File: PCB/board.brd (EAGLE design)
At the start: 30 x 30 mm, 13 parts, among them IC1 W25Q32JVSSIQ, J1 USB-TYPE-C-31-M-17, U1 ESP8266EX, U2 AMS1117_SOT223, Y2 CRYSTAL-26MHZ

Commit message: schematics
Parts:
- removed Y2: CRYSTAL-26MHZ, angrypig7-Clocks:CRYSTAL-SMD-3.2X2.5MM
- added C10: 100nF, angrypig7-RCL:C0402
- added C11, C12: 1uF, angrypig7-RCL:C0402
- added C13: 10uF, angrypig7-RCL:C0402
- added C14: 5.6pF, angrypig7-RCL:C0402
- added C8: 20pF, angrypig7-RCL:C0402
- added R1: (no value), angrypig7-RCL:R0402
- added R2: 12k, angrypig7-RCL:R0402
- added U3: ESP01_PINOUT, angrypig7-IC:ESP01-PINOUT
- added X1: SMA, angrypig7-Connectors:SMA-END-LAUNCH-2
- added Y1: 26Mhz, angrypig7-Clocks:CRYSTAL-SMD-3.2X2.5MM
- C9: value 1uF -> 20pF
- moved IC1 11.3 mm to (15.2, 11.6), turned to 0 degrees
- moved C9 7.11 mm to (20.3, 22.0), turned to 180 degrees
- moved C6 6.13 mm to (3.81, 21.7)
- moved C1 5.21 mm to (9.81, 9.40), turned to 180 degrees
- moved C7 1.85 mm to (19.1, 14.8)
- moved U1 1.38 mm to (15.0, 19.8), turned to 270 degrees
- moved C2 0.92 mm to (5.84, 2.29)
- moved U2 0.92 mm to (4.45, 7.49)
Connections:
- new net ADC_IN: U1.TOUT
- new net CHIP_EN: U1.CHIP_EN, U3.CH_PD
- new net GPIO0: U1.GPIO0, U3.GPIO0
- new net GPIO12: U1.MTDI
- new net GPIO13: U1.MTCK
- new net GPIO14: U1.MTMS
- new net GPIO15: U1.MTDO
- new net GPIO16: U1.XPD_DCDC
- new net GPIO2: U1.GPIO2, U3.GPIO2
- new net GPIO4: U1.GPIO4
- new net GPIO5: U1.GPOIO5
- new net N$1: C9.2, U1.XTAL_IN, Y1.3
- new net N$2: C8.2, U1.XTAL_OUT, Y1.1
- new net N$3: R1.1, U1.SD_CLK
- new net N$4: R2.2, U1.RES12K
- new net N$5: U1.LNA
- new net N$6: X1.1
- new net RST: U1.EXT_RSTB, U3.RST
- new net SD_CLK: IC1.6, R1.2
- new net SD_CMD: IC1.1, U1.SD_CMD
- new net SD_D0: IC1.2, U1.SD_DATA_0
- new net SD_D1: IC1.5, U1.SD_DATA_1
- new net SD_D2: IC1.7, U1.SD_DATA_2
- new net SD_D3: IC1.3, U1.SD_DATA_3
- new net URXD: U1.U0RXD, U3.RX
- new net UTXD: U1.U0TXD, U3.TX
- net 3.3V: now also C10.1, C11.1, C12.1, C13.1, U1.VDD3P3, U1.VDD3P3$2, U1.VDDPST, U1.VDDPST$2, U3.VCC; no longer C9.1
- net GND: now also C10.2, C11.2, C12.2, C13.2, C8.1, C9.1, R2.1, U3.GND, X1.G@1, X1.G@2, X1.G@3, X1.G@4, Y1.2, Y1.4; no longer C9.2

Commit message: added peripherals
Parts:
- removed C1: 1uF, angrypig7-RCL:C0402
- added C15: 1uF, angrypig7-RCL:C0402
- added D1: LED_0603, angrypig7-Diodes:LED_0603
- added R3, R4: 10k, angrypig7-RCL:R0402
- added S1: RST, angrypig7-Switches:TACTILE_SWITCH_SMD_6.0X3.5MM
- added S2: FLASH, angrypig7-Switches:TACTILE_SWITCH_SMD_6.0X3.5MM
- added TP1: TEST-POINT-3, angrypig7-Tests:PAD-3X-RECT-SILK
- R1: value (none) -> 200R
- moved U3 27.5 mm to (2.96, 21.3), turned to 270 degrees
- moved C2 7.00 mm to (1.21, 7.54), turned to 270 degrees
- moved C6 6.92 mm to (9.46, 17.7)
- moved C12 3.61 mm to (26.2, 25.4)
- moved U2 3.13 mm to (5.66, 4.61), turned to 90 degrees
- moved C3 3.00 mm to (7.75, 11.7)
- moved C4 3.00 mm to (5.33, 11.7)
- moved C5 3.00 mm to (2.29, 11.7)
- moved C10 2.70 mm to (17.9, 24.0), turned to 90 degrees
- moved C13 2.09 mm to (19.1, 24.0), turned to 90 degrees
- moved C11 1.99 mm to (9.45, 20.5), turned to 0 degrees
- moved R2 0.76 mm to (20.4, 24.0), turned to 270 degrees
- moved R1 0.25 mm to (16.6, 15.1)
- moved C14 0.24 mm to (14.6, 24.3), turned to 180 degrees
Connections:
- new net N$7: D1.A, R4.1
- net 3.3V: now also C15.1, R3.1, R4.2, TP1.P$2
- net 5V: now also TP1.P$3; no longer C1.1
- net CHIP_EN: now also R3.2, S1.1
- net GND: now also C15.2, D1.C, S1.2, S2.2, TP1.P$1; no longer C1.2
- net GPIO0: now also S2.1
- net N$5: now also C14.1
- net N$6: now also C14.2

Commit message: PCB layout
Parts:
- removed C15: 1uF, angrypig7-RCL:C0402
- removed C9: 20pF, angrypig7-RCL:C0402
- added C1: 1uF, angrypig7-RCL:C0402
- added JP1: (no value), pinhead_v2:1X04/OCT
- C10: value 100nF -> 1uF
- C11, C12: value 1uF -> 20pF
- C13: value 10uF -> 1uF
- C14: value 5.6pF -> 1uF
- C2: value 1uF -> 10uF
- C3: value 10uF -> 5.6pF
- C5: value 100uF -> 10uF; device angrypig7-RCL:SMC_B -> angrypig7-RCL:C0402
- C6: value 1uF -> 100uF; device angrypig7-RCL:C0402 -> angrypig7-RCL:SMC_B
- C7: value 1uF -> 100nF
- C8: value 20pF -> 1uF
- R1: value 200R -> 10k
- R2: value 12k -> 10k
- R3: value 10k -> 12k
- R4: value 10k -> 200R
- U1: value ESP8266EX -> ESP01_PINOUT; device angrypig7-IC:ESP8266EX -> angrypig7-IC:ESP01-PINOUT
- U3: value ESP01_PINOUT -> ESP8266EX; device angrypig7-IC:ESP01-PINOUT -> angrypig7-IC:ESP8266EX
- moved R1 19.3 mm to (2.79, 28.6)
- moved R4 16.3 mm to (12.6, 15.4)
- moved C5 14.7 mm to (10.8, 23.7)
- moved C3 14.4 mm to (15.6, 23.7), turned to 180 degrees
- moved C11 13.0 mm to (21.5, 15.6)
- moved U3 12.1 mm to (15.0, 19.7)
- moved C7 11.0 mm to (12.8, 23.7), turned to 180 degrees
- moved U1 10.6 mm to (4.45, 20.6), flipped to the bottom
- moved C13 10.2 mm to (9.40, 20.6), turned to 0 degrees
- moved C10 9.80 mm to (27.2, 27.2), turned to 270 degrees
- moved C6 9.05 mm to (2.29, 12.2), turned to 270 degrees
- moved C14 8.96 mm to (15.5, 15.4)
- moved C2 8.65 mm to (7.75, 13.2)
- moved R2 6.47 mm to (26.0, 27.2)
- moved C12 6.38 mm to (21.5, 21.1), turned to 180 degrees
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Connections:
- net 3.3V: now also C14.1, C2.1, C5.1, C6.+, C8.1, JP1.4, R1.2, R2.1, U1.VCC, U3.VDD3P3, U3.VDD3P3$2, U3.VDDA, U3.VDDA$2, U3.VDDD, U3.VDDPST, U3.VDDPST$2; no longer C11.1, C12.1, C15.1, C3.1, C5.+, C6.1, R3.1, R4.2, U1.VDD3P3, U1.VDD3P3$2, U1.VDDA, U1.VDDA$2, U1.VDDD, U1.VDDPST, U1.VDDPST$2, U3.VCC
- net 5V: now also C1.1; no longer C2.1
- net ADC_IN: now also U3.TOUT; no longer U1.TOUT
- net CHIP_EN: now also R2.2, U1.CH_PD, U3.CHIP_EN; no longer R3.2, U1.CHIP_EN, U3.CH_PD
- net GND: now also C1.2, C11.1, C12.1, C14.2, C5.2, C6.-, C8.2, JP1.1, R3.1; no longer C11.2, C12.2, C15.2, C3.2, C5.-, C6.2, C8.1, C9.1, R2.1
- net GPIO12: now also U3.MTDI; no longer U1.MTDI
- net GPIO13: now also U3.MTCK; no longer U1.MTCK
- net GPIO14: now also U3.MTMS; no longer U1.MTMS
- net GPIO15: now also U3.MTDO; no longer U1.MTDO
- net GPIO16: now also U3.XPD_DCDC; no longer U1.XPD_DCDC
- net GPIO4: now also U3.GPIO4; no longer U1.GPIO4
- net GPIO5: now also U3.GPOIO5; no longer U1.GPOIO5
- net N$1: now also C12.2, U3.XTAL_IN; no longer C9.2, U1.XTAL_IN
- net N$2: now also C11.2, U3.XTAL_OUT; no longer C8.2, U1.XTAL_OUT
- net N$3: now also R4.1, U3.SD_CLK; no longer R1.1, U1.SD_CLK
- net N$4: now also R3.2, U3.RES12K; no longer R2.2, U1.RES12K
- net N$5: now also C3.1, U3.LNA; no longer C14.1, U1.LNA
- net N$6: now also C3.2; no longer C14.2
- net N$7: now also R1.1; no longer R4.1
- net RST: now also U1.RST, U3.EXT_RSTB; no longer U1.EXT_RSTB, U3.RST
- net SD_CLK: now also R4.2; no longer R1.2
- net SD_CMD: now also U3.SD_CMD; no longer U1.SD_CMD
- net SD_D0: now also U3.SD_DATA_0; no longer U1.SD_DATA_0
- net SD_D1: now also U3.SD_DATA_1; no longer U1.SD_DATA_1
- net SD_D2: now also U3.SD_DATA_2; no longer U1.SD_DATA_2
- net SD_D3: now also U3.SD_DATA_3; no longer U1.SD_DATA_3
- net URXD: now also JP1.3, U1.RX, U3.U0RXD; no longer U1.U0RXD, U3.RX
- net UTXD: now also JP1.2, U1.TX, U3.U0TXD; no longer U1.U0TXD, U3.TX

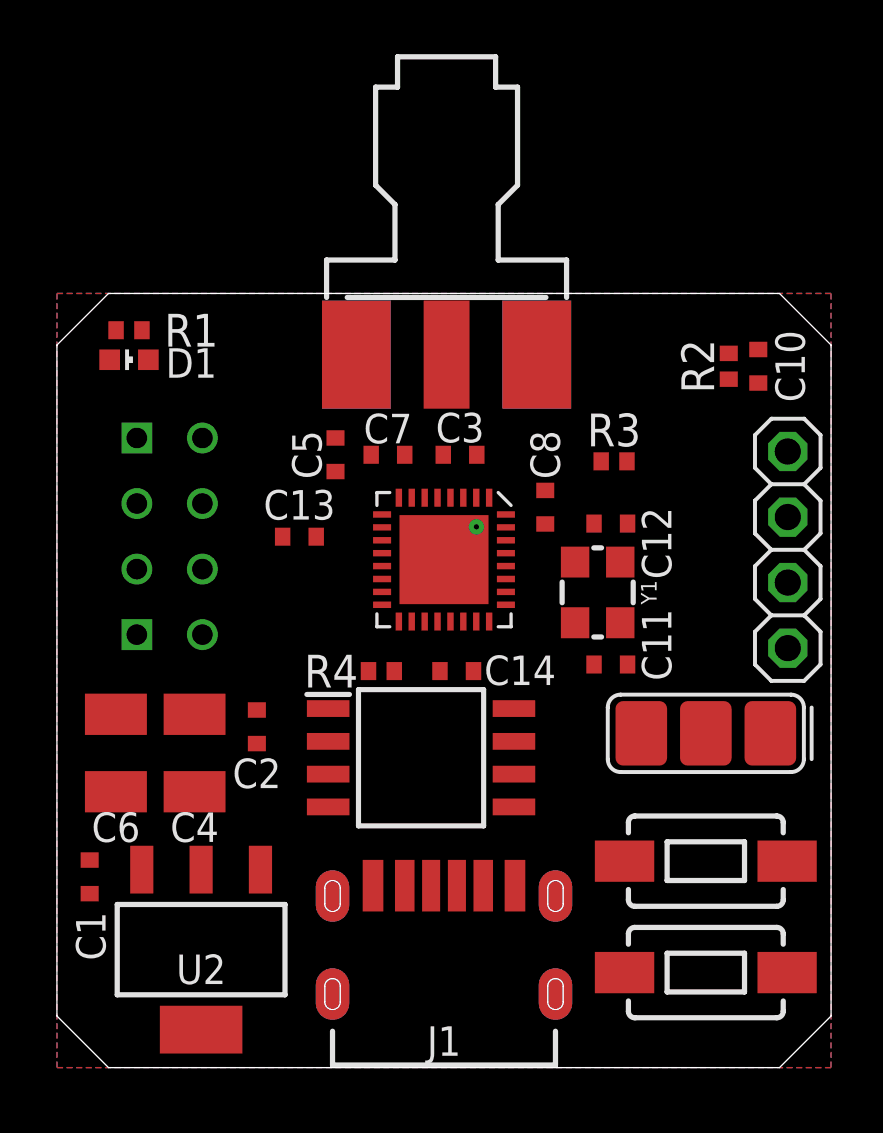
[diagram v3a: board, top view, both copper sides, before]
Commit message: added CH340
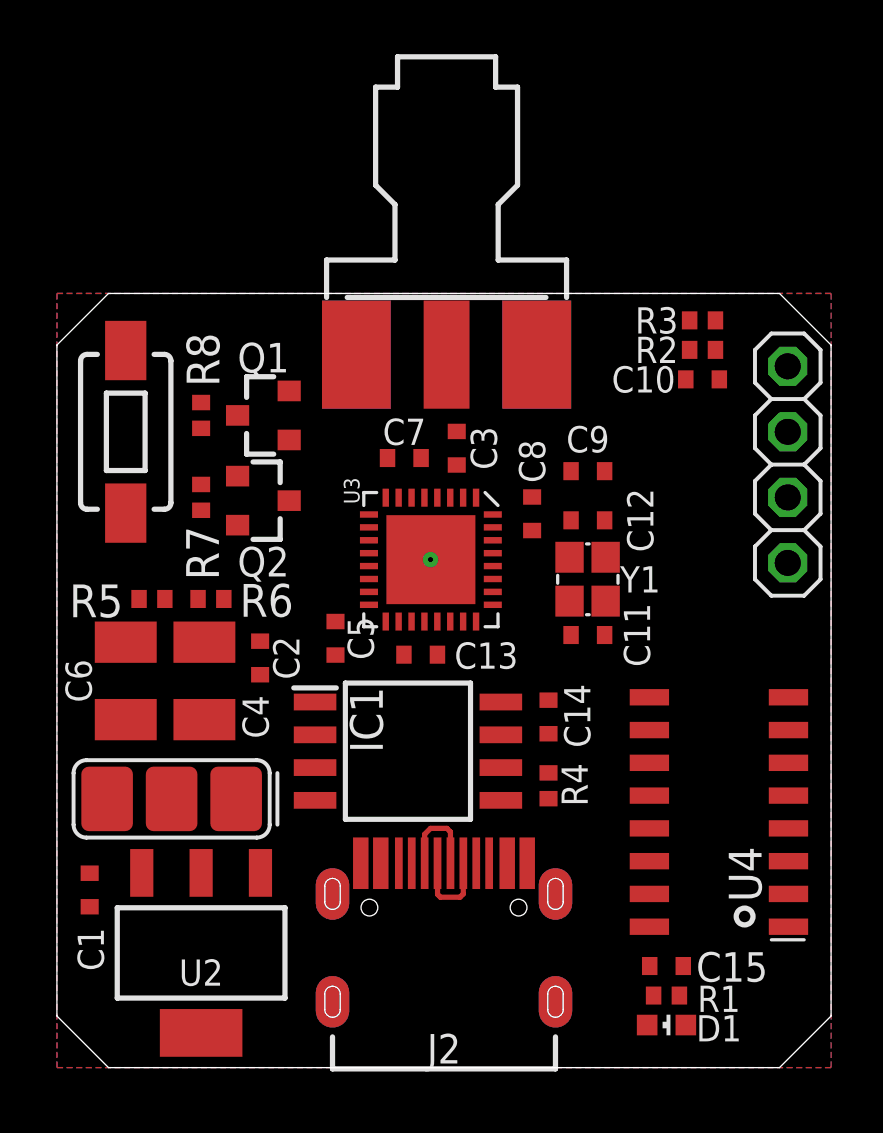
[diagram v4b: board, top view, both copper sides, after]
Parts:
- removed J1: USB-TYPE-C-31-M-17, angrypig7-Connectors:USB-TYPE-C-31-M-17
- removed S2: FLASH, angrypig7-Switches:TACTILE_SWITCH_SMD_6.0X3.5MM
- removed U1: ESP01_PINOUT, angrypig7-IC:ESP01-PINOUT
- added C15, C9: 10uF, angrypig7-RCL:C0402
- added J2: USB-TYPE-C-31-M-12, angrypig7-Connectors:USB-TYPE-C-31-M-12
- added Q1, Q2: S8050, angrypig7-Transistors:SOT-23-3
- added R5, R6: 10k, angrypig7-RCL:R0402
- added R7, R8: 4.7k, angrypig7-RCL:R0402
- added U4: CH340G, angrypig7-IC:SOIC16
- C10: value 1uF -> 100nF
- C11, C12: value 20pF -> 15pF
- R2: value 10k -> 1k
- R3: value 12k -> 12k, 1%
- Y1: value 26Mhz -> 40Mhz; device angrypig7-Clocks:CRYSTAL-SMD-3.2X2.5MM -> angrypig7-Clocks:CRYSTAL-SMD-2X2.5MM
- moved D1 33.1 mm to (23.6, 1.65), turned to 0 degrees
- moved R1 33.1 mm to (23.6, 2.79), turned to 180 degrees
- moved S1 30.7 mm to (2.67, 24.6), turned to 270 degrees
- moved TP1 20.9 mm to (4.45, 10.4)
- moved R4 7.86 mm to (19.1, 10.9), turned to 270 degrees
- moved C5 7.11 mm to (10.8, 16.6), turned to 270 degrees
- moved C13 6.56 mm to (14.1, 16.0)
- moved R3 6.45 mm to (25.0, 29.0)
- moved C14 3.98 mm to (19.1, 13.6), turned to 270 degrees
- moved JP1 3.30 mm to (28.3, 23.4)
- moved C4 2.82 mm to (5.71, 15.0)
- moved C6 2.82 mm to (2.67, 15.0)
- moved C2 2.67 mm to (7.87, 15.9)
- moved C10 2.22 mm to (25.0, 26.7), turned to 180 degrees
- moved C11 1.45 mm to (20.6, 16.8)
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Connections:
- new net DTR: Q2.2, R7.2
- new net DTS: U4.13
- new net N$8: Q1.1, R7.1
- new net N$9: Q2.1, R8.1
- new net RTS: Q1.2, R8.2, U4.14
- new net USB_D+: J2.A6, J2.B6, U4.5
- new net USB_D-: J2.A7, J2.B7, U4.6
- net 3.3V: now also C15.1, C9.1, R2.2, R5.2, R6.2, U4.16; no longer C10.1, R2.1, U1.VCC
- net 5V: now also J2.VBUS1, J2.VBUS2; no longer J1.VBUS, J1.VBUS_2
- net CHIP_EN: now also C10.1, R2.1; no longer R2.2, U1.CH_PD
- net GND: now also C15.2, C9.2, J2.GND1, J2.GND2, J2.SHLD-B1, J2.SHLD-B2, J2.SHLD-B3, J2.SHLD-B4, J2.SHLD-T1, J2.SHLD-T2, J2.SHLD-T3, J2.SHLD-T4, U4.1, Y1.P2, Y1.P4; no longer J1.GND, J1.GND_2, J1.SHLD-B1, J1.SHLD-B2, J1.SHLD-B3, J1.SHLD-B4, J1.SHLD-T1, J1.SHLD-T2, J1.SHLD-T3, J1.SHLD-T4, S2.2, U1.GND, Y1.2, Y1.4
- net GPIO0: now also Q2.3, R5.1; no longer S2.1, U1.GPIO0
- net GPIO2: now also R6.1; no longer U1.GPIO2
- net N$1: now also Y1.P3; no longer Y1.3
- net N$2: now also Y1.P1; no longer Y1.1
- net RST: now also Q1.3; no longer U1.RST
- net URXD: now also U4.2; no longer U1.RX
- net UTXD: now also U4.3; no longer U1.TX
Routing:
- net USB_D+: track 0.00 -> 3.49 mm
- net USB_D-: track 0.00 -> 3.49 mm
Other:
- board text added: "3V3"
- board text added: "GND"
- board text added: "RX"
- board text added: "TX"

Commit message: first version, added gerbers and BOM
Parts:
- removed U4: CH340G, angrypig7-IC:SOIC16
- added C16: 100uF, angrypig7-RCL:SMC_B
- added U1: AMS1117_SOT223, angrypig7-IC-Power:SOT-223
- C11: value 15pF -> 10uF
- C12: value 15pF -> 5.6pF
- C15: value 10uF -> 100nF
- C3: value 5.6pF -> 100uF; device angrypig7-RCL:C0402 -> angrypig7-RCL:SMC_B
- C5: value 10uF -> 15pF
- C6: value 100uF -> 15pF; device angrypig7-RCL:SMC_B -> angrypig7-RCL:C0402
- C7: value 100nF -> 10uF
- R1: value 10k -> 12k,1%
- R2: value 1k -> 4.7k
- R3: value 12k, 1% -> 4.7k
- R7: value 4.7k -> 10k
- R8: value 4.7k -> 1k
- U2: value AMS1117_SOT223 -> CH340G; device angrypig7-IC-Power:SOT-223 -> angrypig7-IC:SOIC16
- moved R7 26.4 mm to (23.6, 2.79), turned to 180 degrees
- moved R1 26.2 mm to (25.0, 29.0)
- moved C15 22.8 mm to (25.0, 26.7), turned to 180 degrees
- moved U2 20.8 mm to (25.7, 9.91)
- moved R2 20.3 mm to (5.59, 22.1), turned to 270 degrees
- moved R3 19.8 mm to (5.59, 25.3), turned to 90 degrees
- moved R8 19.6 mm to (25.0, 27.8), turned to 180 degrees
- moved C6 19.0 mm to (20.6, 21.2), turned to 180 degrees
- moved C3 13.3 mm to (5.71, 15.0)
- moved C11 13.2 mm to (23.6, 3.94)
- moved C10 12.3 mm to (13.1, 23.7)
- moved C9 9.95 mm to (10.6, 23.7), turned to 180 degrees
- moved C5 9.78 mm to (20.6, 16.8), turned to 0 degrees
- moved C7 6.23 mm to (19.6, 22.4), turned to 0 degrees
- moved C12 5.80 mm to (15.5, 24.0), turned to 90 degrees
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- renumbered J2 to J1
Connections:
- removed net USB_D+: J1.A6, J1.B6, U4.5
- removed net USB_D-: J1.A7, J1.B7, U4.6
- new net USB_N: J1.A7, J1.B7, U2.6
- new net USB_P: J1.A6, J1.B6, U2.5
- net 3.3V: now also C10.1, C11.1, C16.+, C3.+, R7.2, R8.2, U1.2, U1.4, U2.16; no longer C15.1, C5.1, C6.+, R1.2, R2.2, U2.2, U2.4, U4.16
- net 5V: now also U1.3; no longer U2.3
- net CHIP_EN: now also C15.1, R8.1; no longer C10.1, R2.1
- net DTR: now also R2.2; no longer R7.2
- net DTS: now also U2.13; no longer U4.13
- net GND: now also C11.2, C16.-, C3.-, C5.1, C6.1, R1.1, U1.1; no longer C11.1, C12.1, C5.2, C6.-, R3.1, U4.1
- net N$1: now also C6.2; no longer C12.2
- net N$2: now also C5.2; no longer C11.2
- net N$4: now also R1.2; no longer R3.2
- net N$5: now also C12.1; no longer C3.1
- net N$6: now also C12.2; no longer C3.2
- net N$7: now also R7.1; no longer R1.1
- net N$8: now also R2.1; no longer R7.1
- net N$9: now also R3.1; no longer R8.1
- net RTS: now also R3.2, U2.14; no longer R8.2, U4.14
- net URXD: now also U2.2; no longer U4.2
- net UTXD: now also U2.3; no longer U4.3
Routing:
- net 3.3V: track 0.00 -> 111.9 mm, vias 0 -> 4
- net CHIP_EN: track 0.00 -> 86.0 mm, vias 0 -> 3
- net UTXD: track 0.00 -> 48.2 mm, vias 0 -> 3
- net URXD: track 0.00 -> 46.4 mm, vias 0 -> 3
- net RTS: track 0.00 -> 42.1 mm, vias 0 -> 2
- net RST: track 0.00 -> 41.3 mm, vias 0 -> 4
- net 5V: track 0.00 -> 27.5 mm, vias 0 -> 2
- net USB_N: track 0.00 -> 19.0 mm, vias 0 -> 2
- net USB_P: track 0.00 -> 18.6 mm, vias 0 -> 2
- net N$4: track 0.00 -> 13.0 mm, vias 0 -> 2
- net GPIO0: track 0.00 -> 12.9 mm, vias 0 -> 2
- net N$3: track 0.00 -> 10.9 mm, vias 0 -> 2
- net SD_D3: track 0.00 -> 10.7 mm
- net SD_D0: track 0.00 -> 9.07 mm
- net SD_D2: track 0.00 -> 8.64 mm, vias 0 -> 2
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
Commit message: CH340C
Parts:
- U2: value CH340G -> CH340C
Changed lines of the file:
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@@
 <setting verticaltext="up"/>
 </settings>
-<grid distance="5" unitdist="mil" unit="mil" style="lines" multiple="1" display="yes" altdistance="5" altunitdist="mil" altunit="mil"/>
+<grid distance="10" unitdist="mil" unit="mil" style="lines" multiple="1" display="yes" altdistance="5" altunitdist="mil" altunit="mil"/>
 <layers>
 <layer number="1" name="Top" color="4" fill="1" visible="yes" active="yes"/>
@@
 <attribute name="SPICEPREFIX" value="R" x="4.318" y="18.161" size="1.143" layer="27" font="vector" ratio="15" rot="R180" display="off"/>
 </element>
-<element name="U2" library="angrypig7-IC" package="SOIC16" value="CH340G" x="25.654" y="9.906" smashed="yes" rot="R90">
+<element name="U2" library="angrypig7-IC" package="SOIC16" value="CH340C" x="25.654" y="9.906" smashed="yes" rot="R90">
 <attribute name="LCSC" value="C14267" x="25.654" y="9.906" size="1.778" layer="27" rot="R90" display="off"/>
-<attribute name="NAME" x="26.67" y="7.493" size="1.27" layer="25" font="vector" ratio="15" rot="R270" align="center"/>
+<attribute name="NAME" x="25.019" y="13.97" size="1.27" layer="25" font="vector" ratio="15" align="center"/>
 </element>
 <element name="J1" library="angrypig7-Connectors" package="USB-TYPE-C-31-M-12" value="USB-TYPE-C-31-M-12" x="15" y="6.731" smashed="yes">

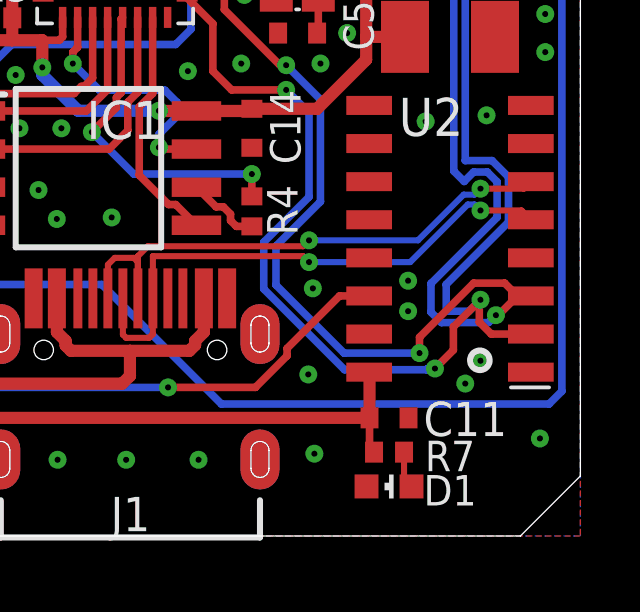
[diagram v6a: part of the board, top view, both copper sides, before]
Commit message: CH340C - V3 pin wiring error
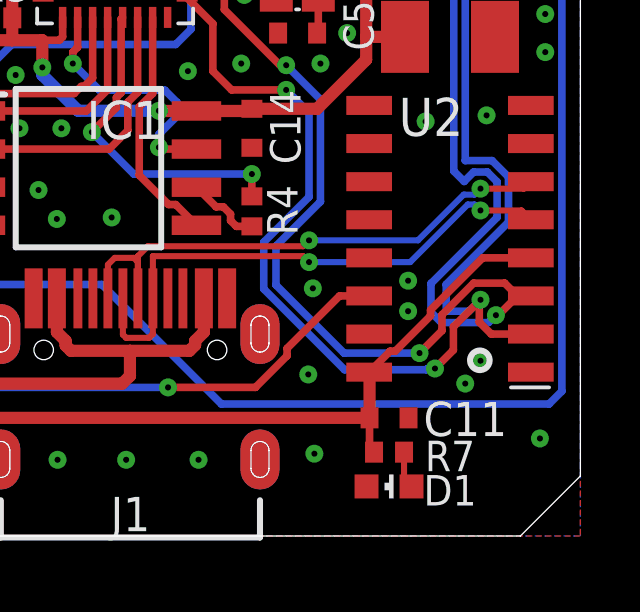
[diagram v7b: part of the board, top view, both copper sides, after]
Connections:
- net 3.3V: now also U2.4
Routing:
- net 3.3V: track 111.9 -> 119.0 mm
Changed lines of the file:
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@@
 <wire x1="13.7056" y1="23.114" x2="11.3792" y2="23.114" width="0.254" layer="1"/>
 <wire x1="18.923" y1="23.353" x2="22.86" y2="23.353" width="0.4064" layer="1"/>
+<contactref element="U2" pad="4"/>
+<wire x1="22.959" y1="5.461" x2="23.6575" y2="6.1595" width="0.254" layer="1"/>
+<wire x1="23.6575" y1="6.1595" x2="23.8262125" y2="6.1595" width="0.254" layer="1"/>
+<wire x1="25.00515625" y1="7.5314625" x2="26.74469375" y2="9.271" width="0.254" layer="1"/>
+<wire x1="26.74469375" y1="9.271" x2="28.349" y2="9.271" width="0.254" layer="1"/>
+<wire x1="23.8262125" y1="6.1595" x2="25.00515625" y2="7.33844375" width="0.254" layer="1"/>
+<wire x1="25.00515625" y1="7.33844375" x2="25.00515625" y2="7.5314625" width="0.254" layer="1"/>
 </signal>
 <signal name="N$2">
@@
 <wire x1="27.477496875" y1="8.428003125" x2="27.9045" y2="8.001" width="0.254" layer="1"/>
 <wire x1="26.44051875" y1="8.428003125" x2="27.477496875" y2="8.428003125" width="0.254" layer="1"/>
-<wire x1="24.638" y1="6.625484375" x2="26.44051875" y2="8.428003125" width="0.254" layer="1"/>
-<wire x1="24.638" y1="6.096" x2="24.638" y2="6.625484375" width="0.254" layer="1"/>
 <wire x1="16.892" y1="18.435" x2="17.78881875" y2="18.435" width="0.254" layer="1"/>
 <wire x1="17.78881875" y1="18.435" x2="18.131" y2="18.09281875" width="0.254" layer="1"/>
@@
 <wire x1="21.336" y1="14.5494" x2="20.193" y2="15.6924" width="0.254" layer="16"/>
 <wire x1="21.336" y1="11.145175" x2="21.336" y2="14.5494" width="0.254" layer="16"/>
+<wire x1="24.638" y1="6.096" x2="25.38615625" y2="6.84415625" width="0.254" layer="1"/>
+<wire x1="25.38615625" y1="6.84415625" x2="25.38615625" y2="7.373640625" width="0.254" layer="1"/>
+<wire x1="25.38615625" y1="7.373640625" x2="26.44051875" y2="8.428003125" width="0.254" layer="1"/>
 </signal>
 <signal name="RST">

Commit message: GPIO15 pull-down
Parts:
- added R9: 10k, angrypig7-RCL:R0402
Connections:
- net GND: now also R9.1
- net GPIO15: now also R9.2
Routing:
- net GPIO15: track 0.00 -> 16.6 mm, vias 0 -> 4
- net 3.3V: track 119.0 -> 119.7 mm
